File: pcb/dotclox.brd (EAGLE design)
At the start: 80 x 80 mm, 5 parts, among them IC1 DS1307Z

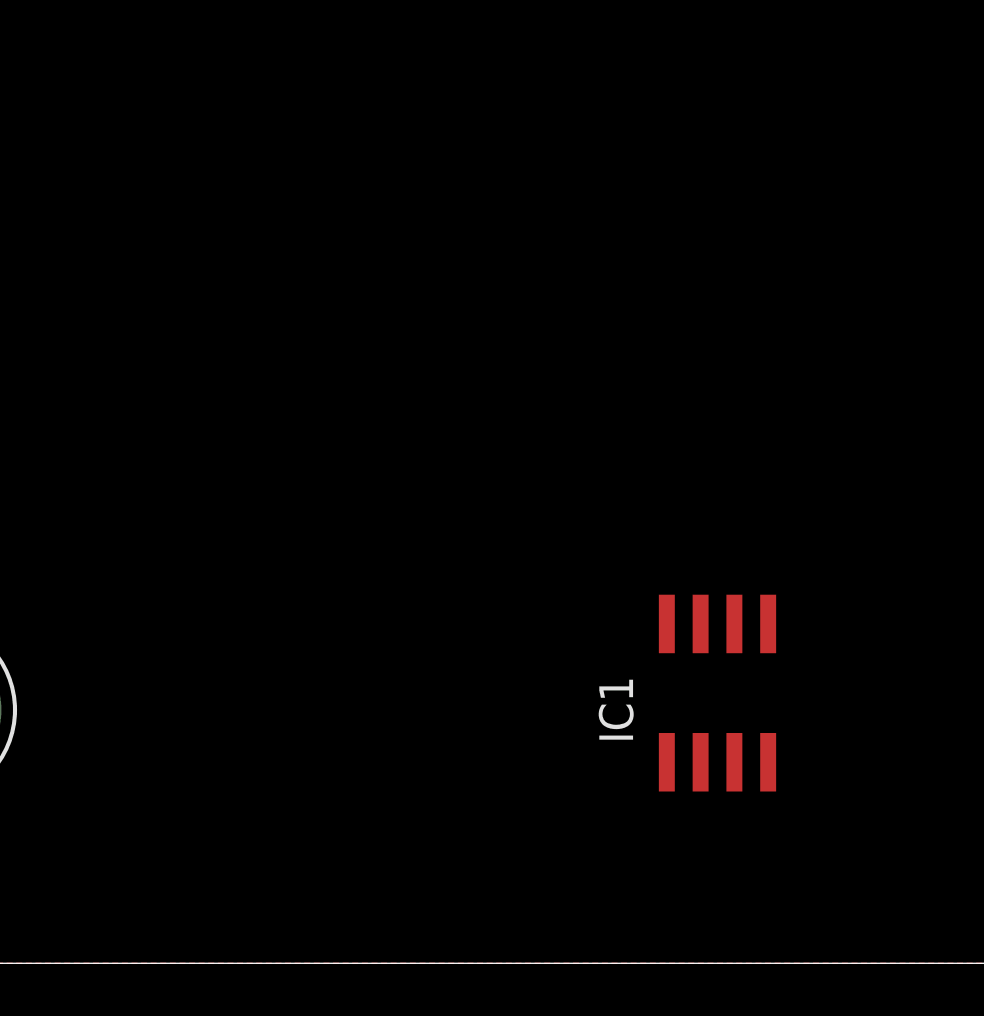
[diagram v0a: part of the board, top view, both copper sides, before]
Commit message: add basic parts to sch and brd
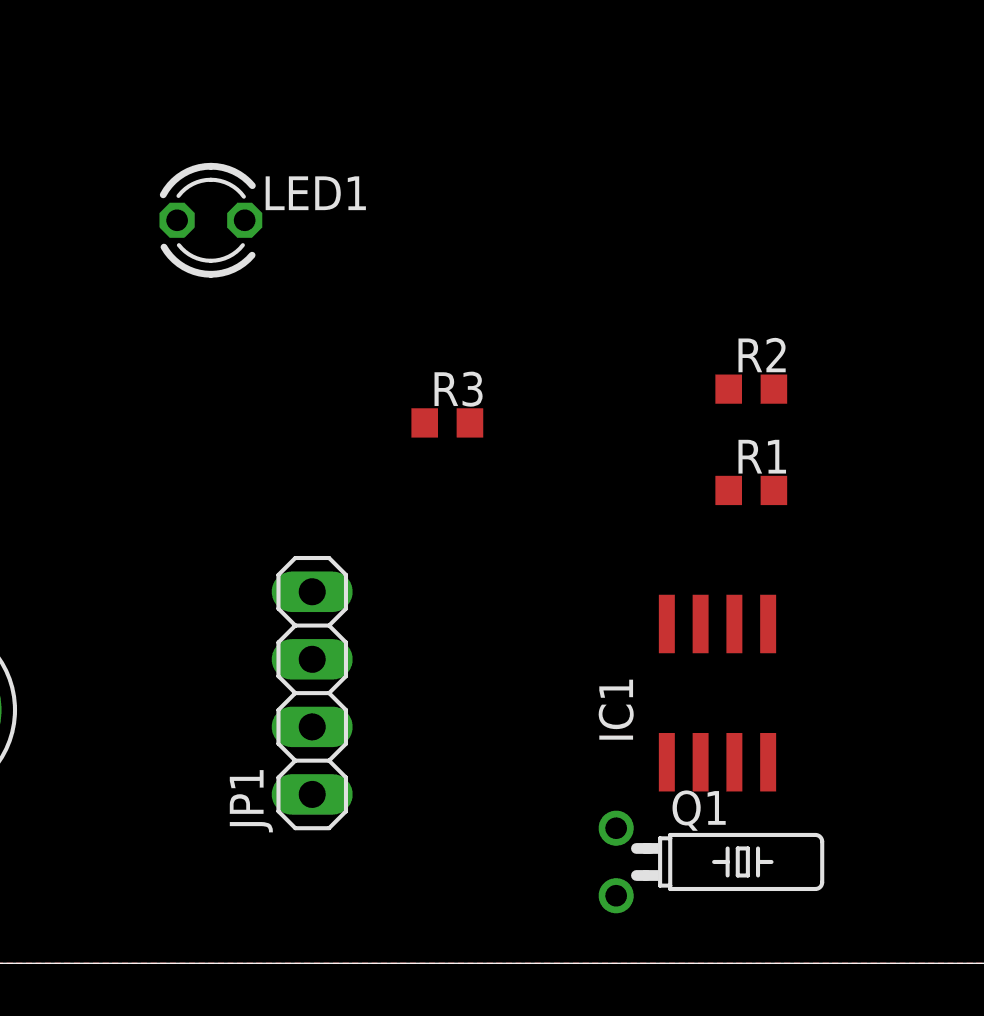
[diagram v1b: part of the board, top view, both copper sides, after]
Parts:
- added JP1: (no value), pinhead:1X04
- added LED1: (no value), led:LED3MM
- added Q1: 32768, crystal:TC26H
- added R1, R2, R3: 1k5, rcl:R0603
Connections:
- new net N$1: IC1.1, Q1.1
- new net N$2: IC1.2, Q1.2
- new net N$3: IC1.6, R3.1
- new net N$4: LED1.K, R3.2
- new net SCL: IC1.7, JP1.4, R1.1
- new net SDA: IC1.8, JP1.3, R2.1
- net GND: now also JP1.1
- net VCC: now also JP1.2, LED1.A, R1.2, R2.2
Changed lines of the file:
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@@
 <?xml version="1.0" encoding="utf-8"?>
 <!DOCTYPE eagle SYSTEM "eagle.dtd">
-<eagle version="7.2.0">
+<eagle version="7.5.0">
 <drawing>
 <settings>
@@
 <setting verticaltext="up"/>
 </settings>
-<grid distance="50" unitdist="mil" unit="mil" style="lines" multiple="1" display="no" altdistance="25" altunitdist="mil" altunit="mil"/>
+<grid distance="25" unitdist="mil" unit="mil" style="dots" multiple="1" display="yes" altdistance="12.5" altunitdist="mil" altunit="mil"/>
 <layers>
 <layer number="1" name="Top" color="4" fill="1" visible="yes" active="yes"/>
@@
 <element name="U$3" library="holes" package="3,2-PAD" value="" x="70.485" y="9.525"/>
 <element name="U$4" library="holes" package="3,2-PAD" value="" x="9.525" y="9.525"/>
+<element name="R1" library="rcl" package="R0603" value="1k5" x="40.64" y="17.78"/>
+<element name="R2" library="rcl" package="R0603" value="1k5" x="40.64" y="21.59"/>
+<element name="JP1" library="pinhead" package="1X04" value="" x="24.13" y="10.16" rot="R90"/>
+<element name="Q1" library="crystal" package="TC26H" value="32768" x="35.56" y="3.81" rot="R270">
+<attribute name="OC_FARNELL" value="unknown" x="35.56" y="3.81" size="1.778" layer="27" rot="R270" display="off"/>
+<attribute name="MF" value="" x="35.56" y="3.81" size="1.778" layer="27" rot="R270" display="off"/>
+<attribute name="MPN" value="" x="35.56" y="3.81" size="1.778" layer="27" rot="R270" display="off"/>
+<attribute name="OC_NEWARK" value="unknown" x="35.56" y="3.81" size="1.778" layer="27" rot="R270" display="off"/>
+</element>
+<element name="R3" library="rcl" package="R0603" value="1k5" x="29.21" y="20.32"/>
+<element name="LED1" library="led" package="LED3MM" value="" x="20.32" y="27.94"/>
 </elements>
 <signals>
@@
 </polygon>
 <contactref element="IC1" pad="4"/>
+<contactref element="JP1" pad="1"/>
+<wire x1="24.13" y1="6.35" x2="41.275" y2="7.56" width="0" layer="19" extent="1-1"/>
 </signal>
 <signal name="VCC">
 <contactref element="IC1" pad="5"/>
+<contactref element="R2" pad="2"/>
+<contactref element="R1" pad="2"/>
+<contactref element="JP1" pad="2"/>
+<contactref element="LED1" pad="A"/>
+<wire x1="41.49" y1="17.78" x2="41.49" y2="21.59" width="0" layer="19" extent="1-1"/>
+<wire x1="41.275" y1="12.76" x2="41.49" y2="17.78" width="0" layer="19" extent="1-1"/>
+<wire x1="24.13" y1="8.89" x2="41.275" y2="12.76" width="0" layer="19" extent="1-1"/>
+<wire x1="19.05" y1="27.94" x2="24.13" y2="8.89" width="0" layer="19" extent="1-1"/>
+</signal>
+<signal name="SCL">
+<contactref element="IC1" pad="7"/>
+<contactref element="R1" pad="1"/>
+<contactref element="JP1" pad="4"/>
+<wire x1="38.735" y1="12.76" x2="39.79" y2="17.78" width="0" layer="19" extent="1-1"/>
+<wire x1="24.13" y1="13.97" x2="38.735" y2="12.76" width="0" layer="19" extent="1-1"/>
+</signal>
+<signal name="SDA">
+<contactref element="IC1" pad="8"/>
+<contactref element="R2" pad="1"/>
+<contactref element="JP1" pad="3"/>
+<wire x1="37.465" y1="12.76" x2="39.79" y2="21.59" width="0" layer="19" extent="1-1"/>
+<wire x1="24.13" y1="11.43" x2="37.465" y2="12.76" width="0" layer="19" extent="1-1"/>
+</signal>
+<signal name="N$1">
+<contactref element="IC1" pad="1"/>
+<contactref element="Q1" pad="1"/>
+<wire x1="35.56" y1="5.08" x2="37.465" y2="7.56" width="0" layer="19" extent="1-1"/>
+</signal>
+<signal name="N$2">
+<contactref element="Q1" pad="2"/>
+<contactref element="IC1" pad="2"/>
+<wire x1="35.56" y1="2.54" x2="38.735" y2="7.56" width="0" layer="19" extent="1-1"/>
+</signal>
+<signal name="N$3">
+<contactref element="IC1" pad="6"/>
+<contactref element="R3" pad="1"/>
+<wire x1="28.36" y1="20.32" x2="40.005" y2="12.76" width="0" layer="19" extent="1-1"/>
+</signal>
+<signal name="N$4">
+<contactref element="R3" pad="2"/>
+<contactref element="LED1" pad="K"/>
+<wire x1="30.06" y1="20.32" x2="21.59" y2="27.94" width="0" layer="19" extent="1-1"/>
 </signal>
 </signals>
